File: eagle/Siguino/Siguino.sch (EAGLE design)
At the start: 49 parts, among them J1 FTDI, J4 10118193-0001LF, J5 U.FL, Q1 MOSFET P-CH 20V 5.3A SOT-23, Q2 MOSFET P-CH 20V 5.3A SOT-23, U1 ATMEGA328P_TQFP, U2 LIS3MDLTR_LIS3MDLTR, U3 SPARKFUN-SENSORS_LIS3DH, U4 BME280, U5 FT232RL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

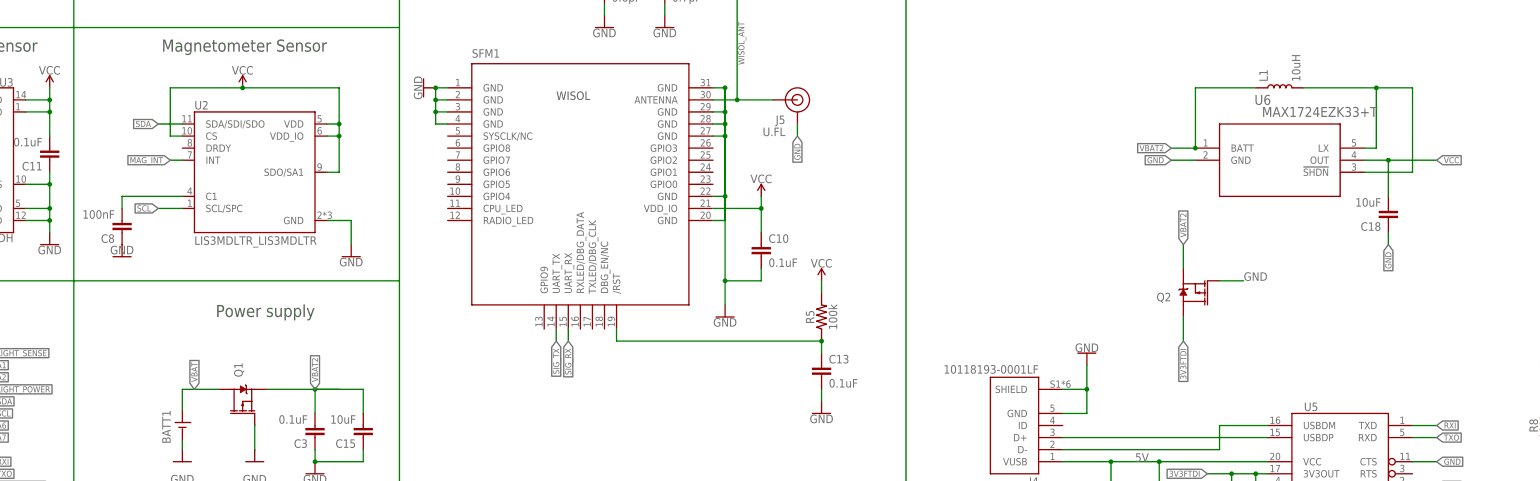
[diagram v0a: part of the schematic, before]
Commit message: Added PPTC over current protection
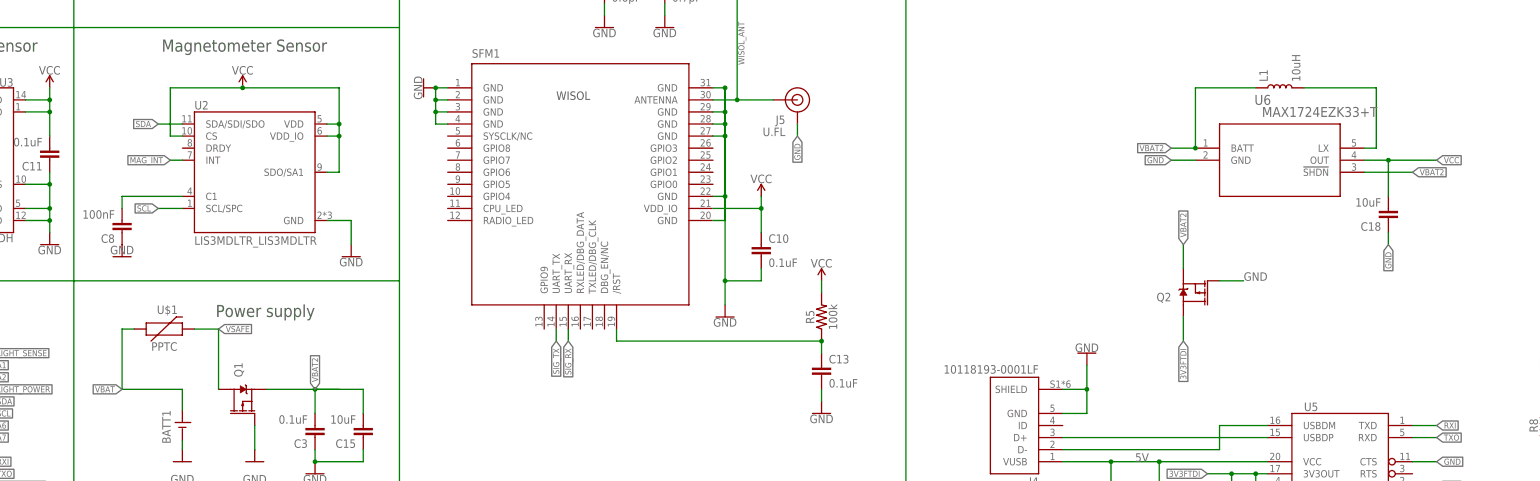
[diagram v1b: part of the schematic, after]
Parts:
- added U$1: PPTC, Siguino:PPTCFUSEGENERIC0603
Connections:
- new net VSAFE: Q1.D, U$1.2
- net N$17: no longer U6.!SHDN
- net VBAT: now also U$1.1; no longer Q1.D
- net VBAT2: now also U6.!SHDN
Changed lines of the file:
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@@
 <part name="Q2" library="SparkFun-DiscreteSemi" deviceset="MOSFET_PCH" device="SI2323DDS" value="MOSFET P-CH 20V 5.3A SOT-23"/>
 <part name="J5" library="SparkFun-Connectors" deviceset="U.FL2PIN" device="" value="U.FL"/>
+<part name="U$1" library="Siguino" deviceset="PPTCFUSEGENERIC0603" device="" value="PPTC"/>
 </parts>
 <sheets>
@@
 <attribute name="NAME" x="271.78" y="114.3" size="1.778" layer="95" rot="MR0"/>
 <attribute name="VALUE" x="271.78" y="111.76" size="1.778" layer="96" rot="MR0"/>
+</instance>
+<instance part="U$1" gate="G$1" x="139.7" y="71.12" smashed="yes">
+<attribute name="NAME" x="141.605" y="74.295" size="1.778" layer="95" font="vector" align="bottom-center"/>
+<attribute name="VALUE" x="140.97" y="68.326" size="1.778" layer="96" font="vector" align="top-center"/>
 </instance>
 </instances>
@@
 <wire x1="246.38" y1="147.32" x2="243.84" y2="147.32" width="0.1524" layer="91"/>
 <junction x="246.38" y="147.32"/>
-</segment>
-</net>
-<net name="VBAT" class="0">
-<segment>
-<pinref part="BATT1" gate="BATT1" pin="VBATT"/>
-<wire x1="144.78" y1="54.02" x2="144.78" y2="58.42" width="0.1524" layer="91"/>
-<wire x1="144.78" y1="58.42" x2="152.4" y2="58.42" width="0.1524" layer="91"/>
-<pinref part="Q1" gate="G$1" pin="D"/>
-<label x="147.32" y="58.42" size="1.27" layer="95" rot="R90" xref="yes"/>
 </segment>
 </net>
@@
 <net name="N$17" class="0">
 <segment>
-<pinref part="U6" gate="A" pin="!SHDN"/>
-<wire x1="393.7" y1="104.14" x2="403.86" y2="104.14" width="0.1524" layer="91"/>
-<wire x1="403.86" y1="104.14" x2="403.86" y2="121.92" width="0.1524" layer="91"/>
 <pinref part="U6" gate="A" pin="LX"/>
 <wire x1="393.7" y1="109.22" x2="396.24" y2="109.22" width="0.1524" layer="91"/>
@@
 <wire x1="381" y1="121.92" x2="396.24" y2="121.92" width="0.1524" layer="91"/>
 <wire x1="396.24" y1="121.92" x2="396.24" y2="109.22" width="0.1524" layer="91"/>
-<wire x1="403.86" y1="121.92" x2="396.24" y2="121.92" width="0.1524" layer="91"/>
-<junction x="396.24" y="121.92"/>
 </segment>
 </net>
@@
 <wire x1="15.24" y1="116.84" x2="17.78" y2="116.84" width="0.1524" layer="91"/>
 <label x="17.78" y="116.84" size="1.27" layer="95" xref="yes"/>
+</segment>
+<segment>
+<pinref part="U6" gate="A" pin="!SHDN"/>
+<wire x1="393.7" y1="104.14" x2="403.86" y2="104.14" width="0.1524" layer="91"/>
+<label x="403.86" y="104.14" size="1.27" layer="95" xref="yes"/>
 </segment>
 </net>
@@
 </segment>
 </net>
+<net name="VBAT" class="0">
+<segment>
+<pinref part="BATT1" gate="BATT1" pin="VBATT"/>
+<wire x1="144.78" y1="54.02" x2="144.78" y2="58.42" width="0.1524" layer="91"/>
+<wire x1="144.78" y1="58.42" x2="132.08" y2="58.42" width="0.1524" layer="91"/>
+<pinref part="U$1" gate="G$1" pin="1"/>
+<wire x1="132.08" y1="58.42" x2="132.08" y2="71.12" width="0.1524" layer="91"/>
+<wire x1="132.08" y1="71.12" x2="134.62" y2="71.12" width="0.1524" layer="91"/>
+<label x="132.08" y="58.42" size="1.27" layer="95" rot="R180" xref="yes"/>
+</segment>
+</net>
+<net name="VSAFE" class="0">
+<segment>
+<pinref part="U$1" gate="G$1" pin="2"/>
+<wire x1="147.32" y1="71.12" x2="152.4" y2="71.12" width="0.1524" layer="91"/>
+<pinref part="Q1" gate="G$1" pin="D"/>
+<wire x1="152.4" y1="71.12" x2="152.4" y2="58.42" width="0.1524" layer="91"/>
+<label x="152.4" y="71.12" size="1.27" layer="95" xref="yes"/>
+</segment>
+</net>
